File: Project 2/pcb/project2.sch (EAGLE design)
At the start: 5 parts, among them SW1 PUSH_BUTTON, U1 POCKETBEAGLE

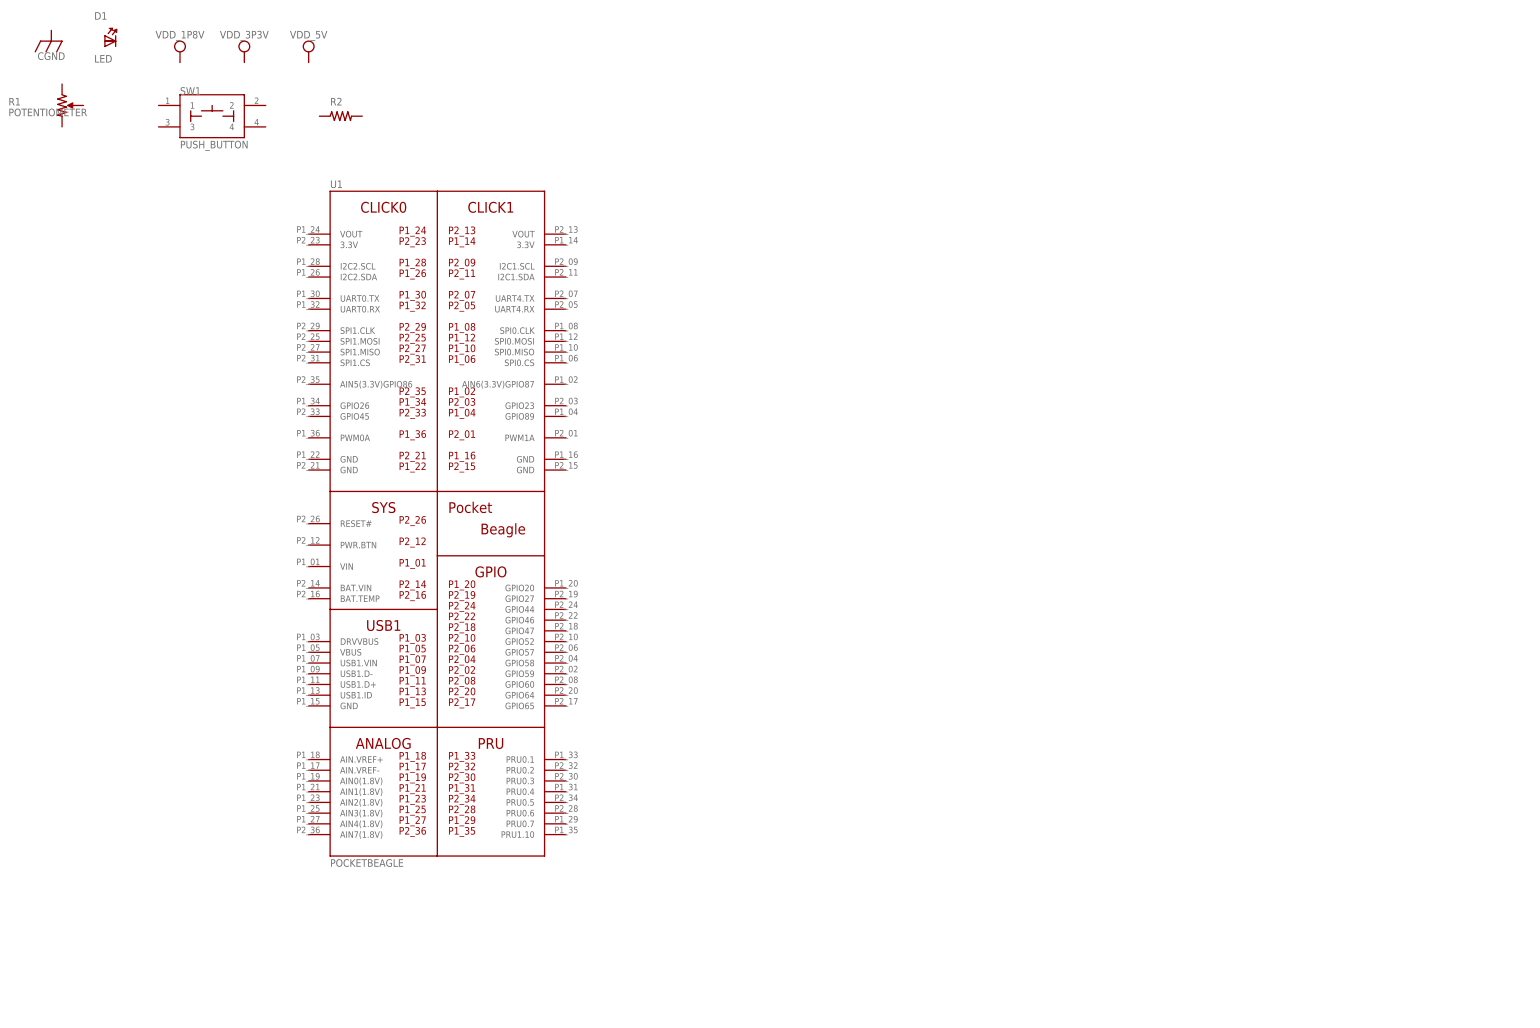
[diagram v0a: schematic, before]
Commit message: Sunday night update
SPI board throwing errors, MacroFab website cannot process .brd as a result.
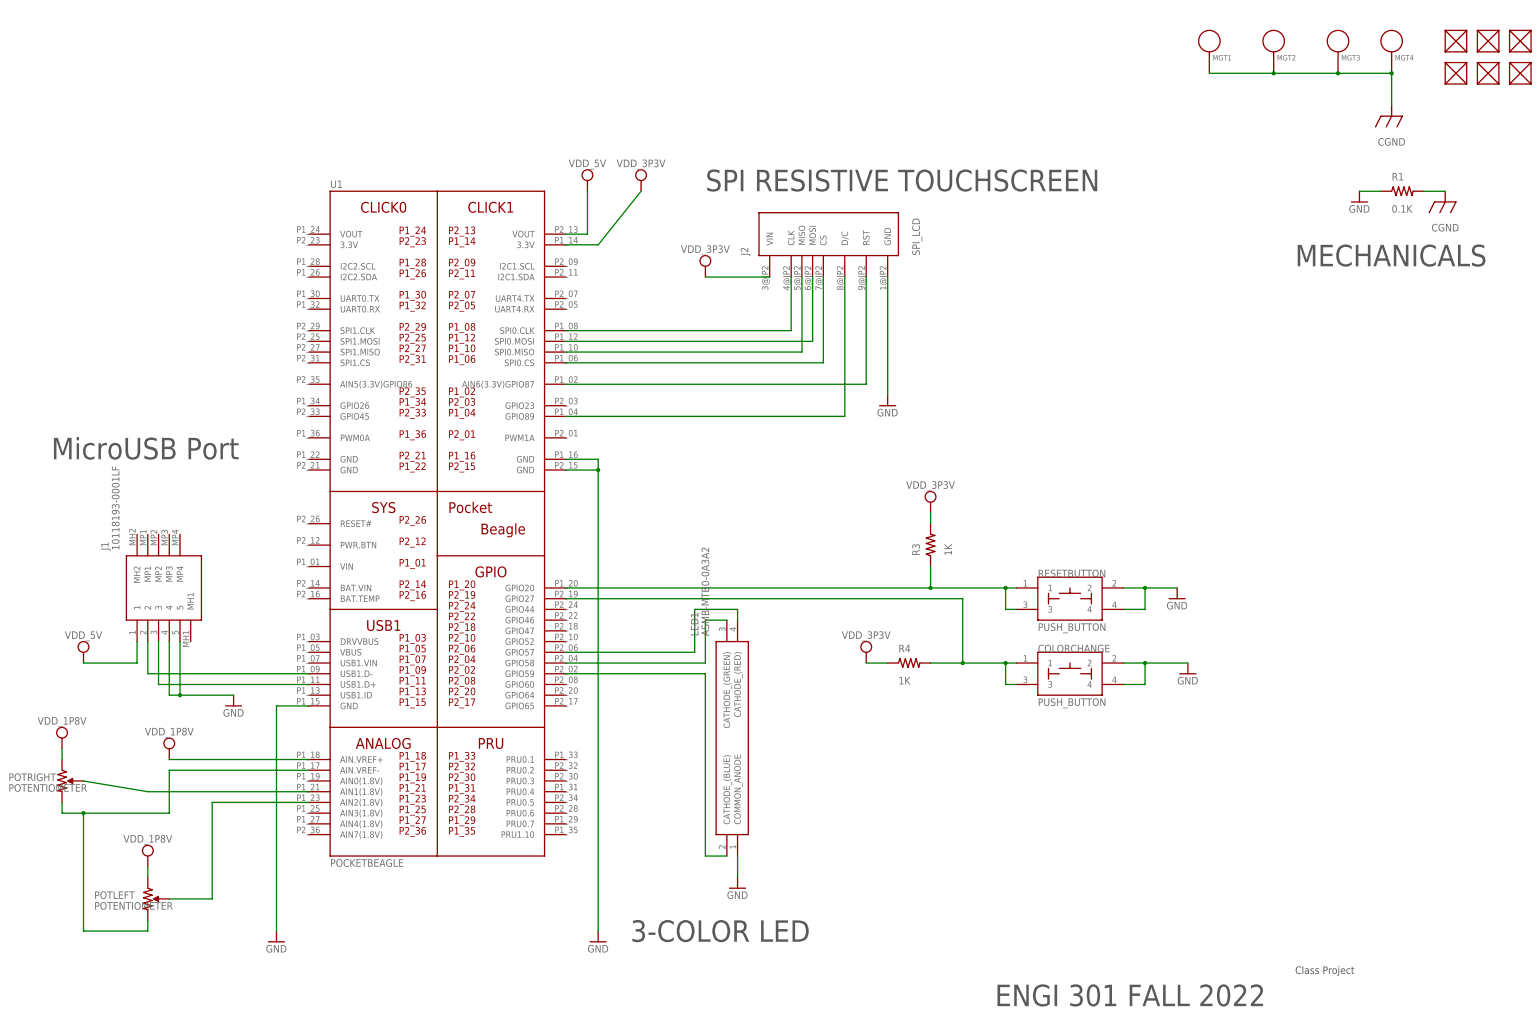
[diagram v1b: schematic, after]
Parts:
- removed D1: LED, project2lib:LED
- removed R2: (no value), project2lib:R_R0603
- removed SW1: PUSH_BUTTON, project2lib:PUSH_BUTTON
- added COLORCHANGE, RESETBUTTON: PUSH_BUTTON, project2lib:PUSH_BUTTON
- added FUD1, FUD2, FUD3, FUD4, FUD5, FUD6: FIDUCIAL, project2:FIDUCIAL
- added J1: 10118193-0001LF, 10118193-0001LF:10118193-0001LF
- added J2: SPI_LCD, project2:SPI_LCD
- added LED1: ASMB-MTB0-0A3A2, project2lib:ASMB-MTB0-0A3A2
- added MGT1, MGT2, MGT3, MGT4: MOUNTING_HOLE, project2:MOUNTING_HOLE
- added POTLEFT, POTRIGHT: POTENTIOMETER, project2lib:POTENTIOMETER
- added R3, R4: 1K, project2lib:R_R0603
- R1: value POTENTIOMETER -> 0.1K; device project2lib:POTENTIOMETER -> project2:R_R0603
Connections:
- new net CGND: MGT1.P$1, MGT2.P$1, MGT3.P$1, MGT4.P$1, R1.2
- new net GND: COLORCHANGE.2, COLORCHANGE.4, J1.4, J1.5, J2.GND, LED1.COMMON_ANODE, R1.1, RESETBUTTON.2, RESETBUTTON.4, U1.GND@1, U1.GND@2, U1.GND@4
- new net N$1: POTRIGHT.S, U1.AIN1(1.8V)
- new net N$10: J2.RST, U1.AIN6(3.3V)GPIO87
- new net N$12: COLORCHANGE.1, COLORCHANGE.3, R4.2, U1.GPIO27
- new net N$13: LED1.CATHODE_(BLUE), U1.GPIO59
- new net N$14: LED1.CATHODE_(GREEN), U1.GPIO58
- new net N$15: LED1.CATHODE_(RED), U1.GPIO57
- new net N$17: J1.2, U1.USB1.D-
- new net N$18: J1.3, U1.USB1.D+
- new net N$2: POTLEFT.S, U1.AIN2(1.8V)
- new net N$3: POTLEFT.CW, POTRIGHT.CW, U1.AIN.VREF-
- new net N$4: R3.1, RESETBUTTON.1, RESETBUTTON.3, U1.GPIO20
- new net N$5: J2.CLK, U1.SPI0.CLK
- new net N$6: J2.MISO, U1.SPI0.MISO
- new net N$7: J2.MOSI, U1.SPI0.MOSI
- new net N$8: J2.CS, U1.SPI0.CS
- new net N$9: J2.D/C, U1.GPIO89
- new net VDD_1P8V: POTLEFT.CCW, POTRIGHT.CCW, U1.AIN.VREF+
- new net VDD_3P3V: J2.VIN, R3.2, R4.1, U1.3.3V@1
- new net VDD_5V: J1.1, U1.VOUT@2
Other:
- note added: "3-COLOR LED"
- note added: "Class Project"
- note added: "ENGI 301 FALL 2022"
- note added: "MECHANICALS"
- note added: "MicroUSB Port"
- note added: "SPI RESISTIVE TOUCHSCREEN"
